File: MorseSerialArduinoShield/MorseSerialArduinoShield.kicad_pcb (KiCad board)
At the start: 2 copper layers, 76.2 x 54.6 mm, 14 parts, among them J1 HC_05, U1 SC39-11SRWA

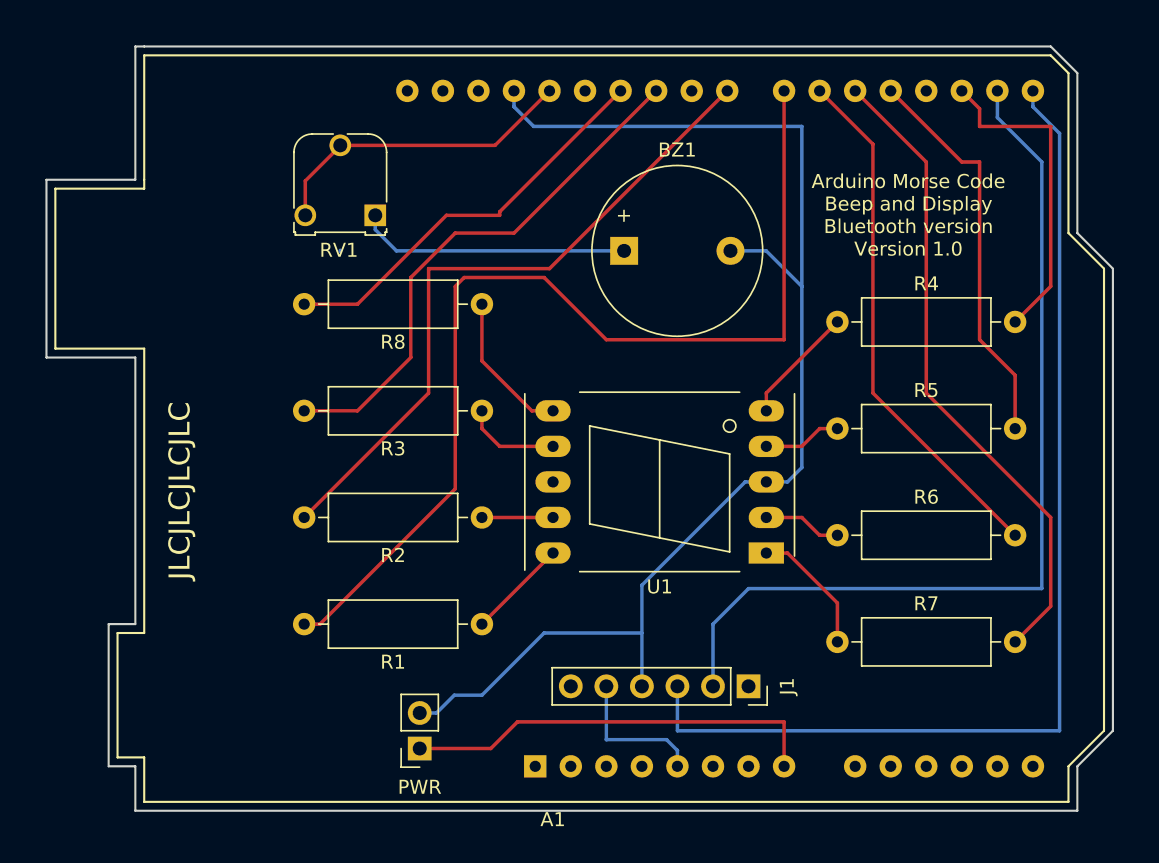
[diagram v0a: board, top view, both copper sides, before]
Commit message: refreshed Gerbers and reassignment of pins
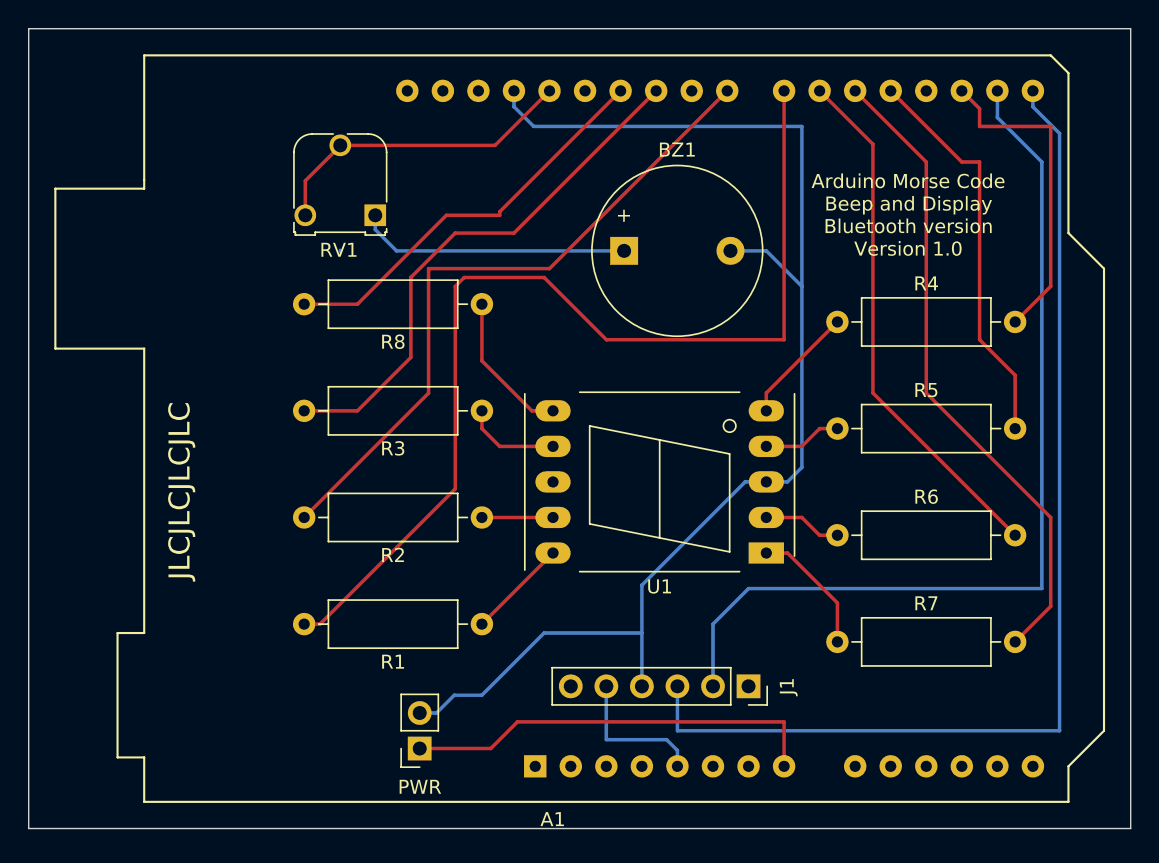
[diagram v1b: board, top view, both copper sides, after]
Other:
- board size 76.2 x 54.6 mm -> 78.7 x 57.2 mm
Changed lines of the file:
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@@
   (general
     (thickness 1.6)
-    (drawings 39)
+    (drawings 25)
     (tracks 104)
     (zones 0)
@@
     )
   )
+  (gr_line (start 181.483 73.66) (end 181.483 130.81) (layer Edge.Cuts) (width 0.1))
+  (gr_line (start 102.743 73.66) (end 181.483 73.66) (layer Edge.Cuts) (width 0.1))
+  (gr_line (start 102.743 130.81) (end 102.743 73.66) (layer Edge.Cuts) (width 0.1))
+  (gr_line (start 181.483 130.81) (end 102.743 130.81) (layer Edge.Cuts) (width 0.1))
   (gr_text JLCJLCJLCJLC (at 113.538 106.68 90) (layer F.SilkS)
     (effects (font (size 1.5 1.5) (thickness 0.3)))
   )
-  (gr_line (start 110.363 74.93) (end 110.998 74.93) (layer Edge.Cuts) (width 0.15))
-  (gr_line (start 110.363 84.455) (end 110.363 74.93) (layer Edge.Cuts) (width 0.15))
-  (gr_line (start 104.013 84.455) (end 110.363 84.455) (layer Edge.Cuts) (width 0.15))
-  (gr_line (start 104.013 97.155) (end 104.013 84.455) (layer Edge.Cuts) (width 0.15))
-  (gr_line (start 110.363 97.155) (end 104.013 97.155) (layer Edge.Cuts) (width 0.15))
-  (gr_line (start 110.363 116.205) (end 110.363 97.155) (layer Edge.Cuts) (width 0.15))
-  (gr_line (start 108.458 116.205) (end 110.363 116.205) (layer Edge.Cuts) (width 0.15))
-  (gr_line (start 108.458 126.365) (end 108.458 116.205) (layer Edge.Cuts) (width 0.15))
-  (gr_line (start 110.363 126.365) (end 108.458 126.365) (layer Edge.Cuts) (width 0.15))
-  (gr_line (start 110.363 129.54) (end 110.363 126.365) (layer Edge.Cuts) (width 0.15))
-  (gr_line (start 177.673 129.54) (end 110.363 129.54) (layer Edge.Cuts) (width 0.15))
-  (gr_line (start 177.673 126.365) (end 177.673 129.54) (layer Edge.Cuts) (width 0.15))
-  (gr_line (start 180.213 123.825) (end 177.673 126.365) (layer Edge.Cuts) (width 0.15))
-  (gr_line (start 180.213 90.805) (end 180.213 123.825) (layer Edge.Cuts) (width 0.15))
-  (gr_line (start 177.673 88.265) (end 180.213 90.805) (layer Edge.Cuts) (width 0.15))
-  (gr_line (start 177.673 76.835) (end 177.673 88.265) (layer Edge.Cuts) (width 0.15))
-  (gr_line (start 175.768 74.93) (end 177.673 76.835) (layer Edge.Cuts) (width 0.15))
-  (gr_line (start 110.998 74.93) (end 175.768 74.93) (layer Edge.Cuts) (width 0.15))
   (gr_line (start 110.998 128.905) (end 177.038 128.905) (layer F.SilkS) (width 0.15))
   (gr_line (start 110.998 125.73) (end 110.998 128.905) (layer F.SilkS) (width 0.15))
